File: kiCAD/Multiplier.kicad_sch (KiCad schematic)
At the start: 58 parts, among them IC2 ADG1221BRMZ, J1 Conn_01x02_Pin, J2 Conn_01x02_Pin, J3 Conn_01x02_Pin, Q7 Q_Dual_PNP_PNP_C1B1B2C2E2E1, Q8 Q_Dual_PNP_PNP_C1B1B2C2E2E1, U1 TS912, U10 TPS63060, U2 TLV340, U4 TS912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

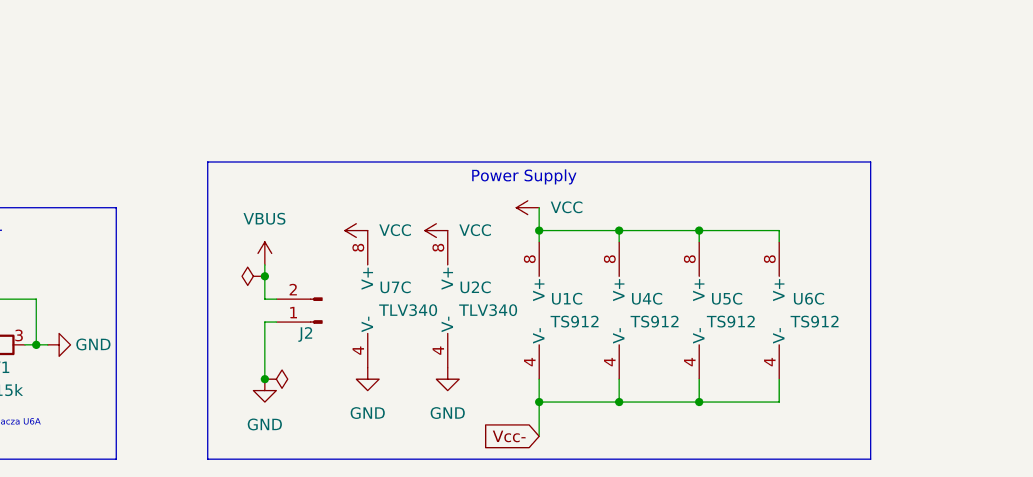
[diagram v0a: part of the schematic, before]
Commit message: New footprint for TSP and tantalum capacitor
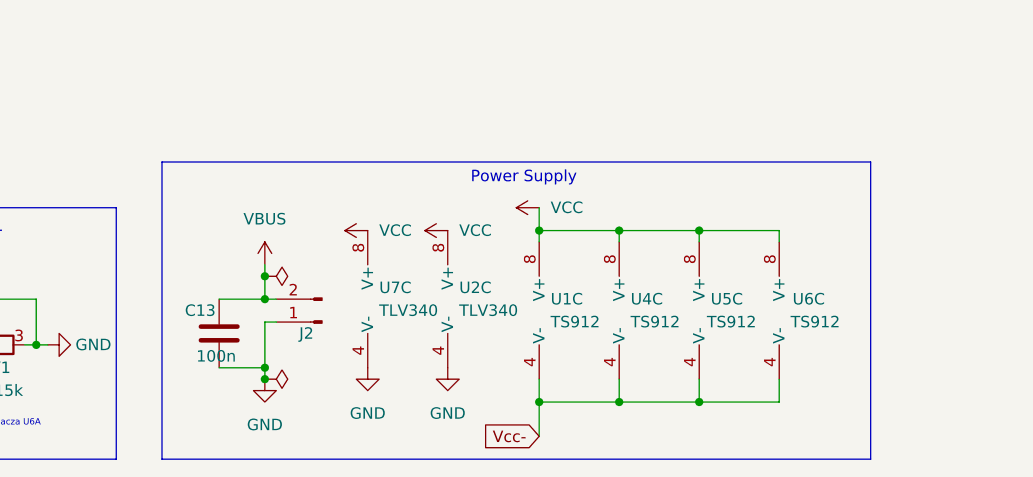
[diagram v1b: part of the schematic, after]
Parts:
- added C13: 100n, Custom:CAP_293D-B_VSS, symbol Device:C
- U10: footprint Package_SON:Texas_S-PWSON-N10_ThermalVias -> Custom:Texas_S-PWSON-N10_ThermalVias_Custom
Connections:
- net GND: now also C13.2
- net VBUS: now also C13.1
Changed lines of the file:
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@@
   (junction (at 199.39 30.48) (diameter 0) (color 0 0 0 0)
   )
+  (junction (at 100.33 175.26) (diameter 0) (color 0 0 0 0)
+  )
   (junction (at 102.87 124.46) (diameter 0) (color 0 0 0 0)
   )
@@
   )
   (junction (at 215.9 57.15) (diameter 0) (color 0 0 0 0)
+  )
+  (junction (at 100.33 182.88) (diameter 0) (color 0 0 0 0)
   )
   (junction (at 234.95 57.15) (diameter 0) (color 0 0 0 0)
@@
     (stroke (width 0) (type default))
   )
+  (wire (pts (xy 95.25 175.26) (xy 100.33 175.26))
+    (stroke (width 0) (type default))
+  )
   (wire (pts (xy 208.28 106.68) (xy 209.55 106.68))
     (stroke (width 0) (type default))
@@
     (stroke (width 0) (type default))
   )
+  (wire (pts (xy 95.25 182.88) (xy 100.33 182.88))
+    (stroke (width 0) (type default))
+  )
   (wire (pts (xy 78.74 33.02) (xy 78.74 35.56))
     (stroke (width 0) (type default))
@@
     (stroke (width 0) (type default))
   )
-  (wire (pts (xy 100.33 177.8) (xy 100.33 184.15))
+  (wire (pts (xy 100.33 177.8) (xy 100.33 182.88))
     (stroke (width 0) (type default))
   )
@@
     (stroke (width 0) (type default))
   )
+  (wire (pts (xy 100.33 182.88) (xy 100.33 184.15))
+    (stroke (width 0) (type default))
+  )
   (wire (pts (xy 233.68 140.97) (xy 236.22 140.97))
     (stroke (width 0) (type default))
@@
     (fill (type none))
   )
-  (rectangle (start 93.98 160.02) (end 167.64 193.04)
+  (rectangle (start 88.9 160.02) (end 167.64 193.04)
     (stroke (width 0) (type default))
     (fill (type none))
@@
     )
   )
-  (symbol (lib_id "power:PWR_FLAG") (at 100.33 172.72 90) (unit 1)
-    (in_bom yes) (on_board yes) (dnp no) (fields_autoplaced)
-    (property "Reference" "#FLG01" (at 98.425 172.72 0)
-      (effects (font (size 1.27 1.27)) hide)
-    )
-    (property "Value" "PWR_FLAG" (at 96.52 172.72 90)
+  (symbol (lib_id "power:PWR_FLAG") (at 100.33 172.72 270) (mirror x) (unit 1)
+    (in_bom yes) (on_board yes) (dnp no)
+    (property "Reference" "#FLG01" (at 102.235 172.72 0)
+      (effects (font (size 1.27 1.27)) hide)
+    )
+    (property "Value" "PWR_FLAG" (at 104.14 172.72 90)
       (effects (font (size 1.27 1.27)) (justify left) hide)
     )
@@
       (effects (font (size 1.27 1.27)))
     )
-    (property "Footprint" "Package_SON:Texas_S-PWSON-N10_ThermalVias" (at 218.44 57.15 0)
+    (property "Footprint" "Custom:Texas_S-PWSON-N10_ThermalVias_Custom" (at 218.44 57.15 0)
       (effects (font (size 1.27 1.27)) hide)
     )
@@
         )
       )
+    )
+  )
+  (symbol (lib_id "Device:C") (at 95.25 179.07 0) (unit 1)
+    (in_bom yes) (on_board yes) (dnp no)
+    (property "Reference" "C13" (at 91.44 176.53 0)
+      (effects (font (size 1.27 1.27)) (justify left))
+    )
+    (property "Value" "100n" (at 92.71 181.61 0)
+      (effects (font (size 1.27 1.27)) (justify left))
+    )
+    (property "Footprint" "Custom:CAP_293D-B_VSS" (at 96.2152 182.88 0)
+      (effects (font (size 1.27 1.27)) hide)
+    )
+    (property "Datasheet" "~" (at 95.25 179.07 0)
+      (effects (font (size 1.27 1.27)) hide)
+    )
+    (pin "1")
+    (pin "2")
+    (instances
+      (project "Multiplier"
+        (path "/8f04f48d-7465-48f4-bbbe-36932343ce91"
+          (reference "C13") (unit 1)
+        )
+      )
